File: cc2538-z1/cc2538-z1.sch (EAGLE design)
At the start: 89 parts, among them Q2 DMG6602SVT, U1 CC2538, U2 CC1120_RHM_32, U3 TPD2E001IDRLRQ1, U4 CP2103, U5 BSS138PS, U6 BSS138PS, U7 BSS138PS, X1 FA-128, X2 32MHz, X3 32.768K

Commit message: A lot of work on 4-layer CC2538/1120 design.
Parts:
- added C16, C17: 100nf, CC11x:C_EUC0603S
- added L5: BEAD, CC11x:L_US0603
- R11, R13: device resistor:R-EU_R0805 -> rcl:R-EU_R0603
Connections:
- removed net N$38: H1.ADC_3V3
- removed net N$47: H1.AGND
- removed net N$63: H1.CDP-3.3V
- new net +3V3_ANALOGUE: C17.1, H1.ADC_3V3, L5.1, U1.AVDD, U1.AVDD2, U1.AVDD3, U1.AVDD4, U1.AVDD5
- new net N$35: H1.ADC0
- new net N$36: H1.ADC3
- new net N$37: H1.ADC4
- new net N$39: H1.ADC6
- new net N$40: H1.ALERT
- net +3V3: now also C16.1, L5.2; no longer U1.AVDD, U1.AVDD2, U1.AVDD3, U1.AVDD4, U1.AVDD5
- net +3V3_SERIAL: now also H1.CDP-3.3V
- net GND: now also C16.2, C17.2, H1.AGND
- net SD_SPI_CLK: now also H1.CA1
- net SD_SPI_MISO: now also H1.TA1
- net SD_SPI_MOSI: now also H1.TA2
- net USER_BUTTON: now also H1.USER_INT
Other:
- moved on the sheet: C12, C13, X3

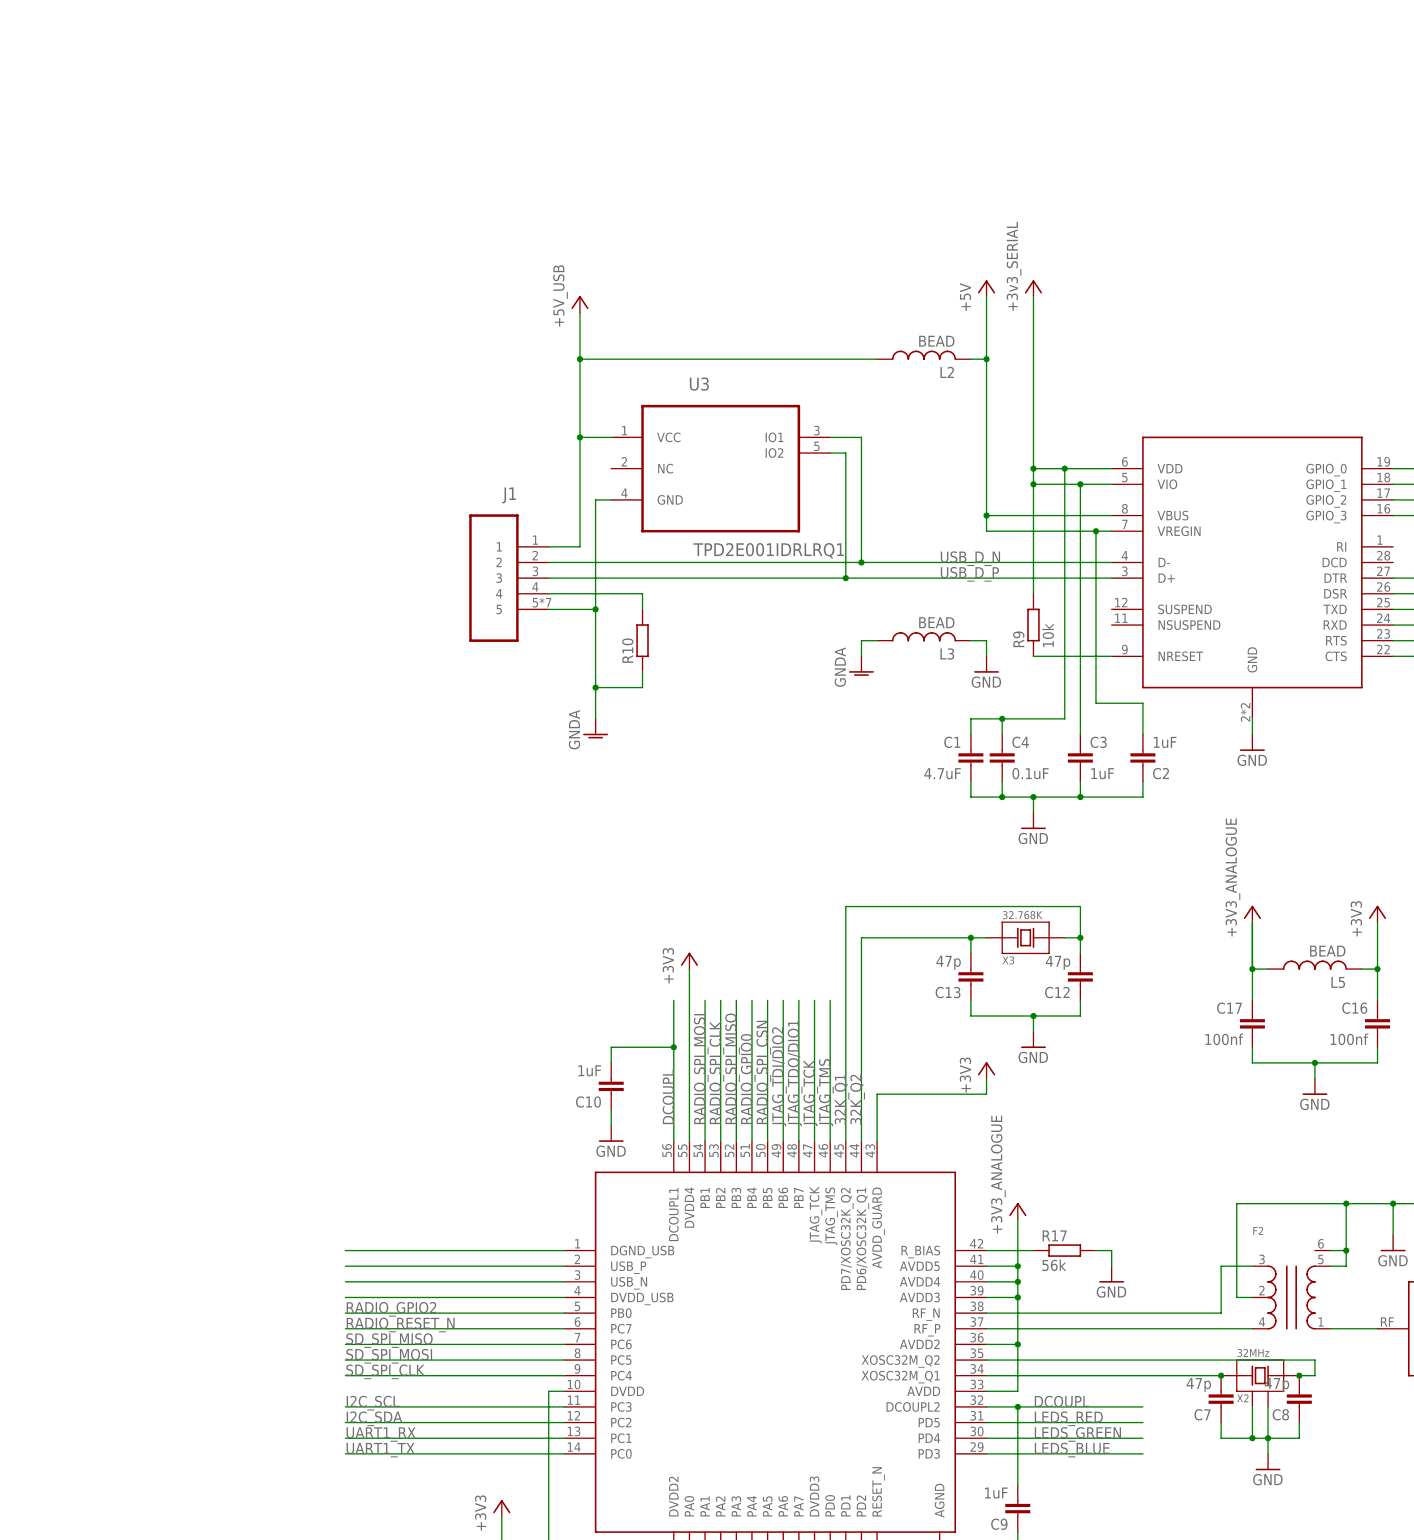
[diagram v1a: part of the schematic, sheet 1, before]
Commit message: Added Serial > 3v3 diode.
Added I2C pullup

still need to work out SD SEL
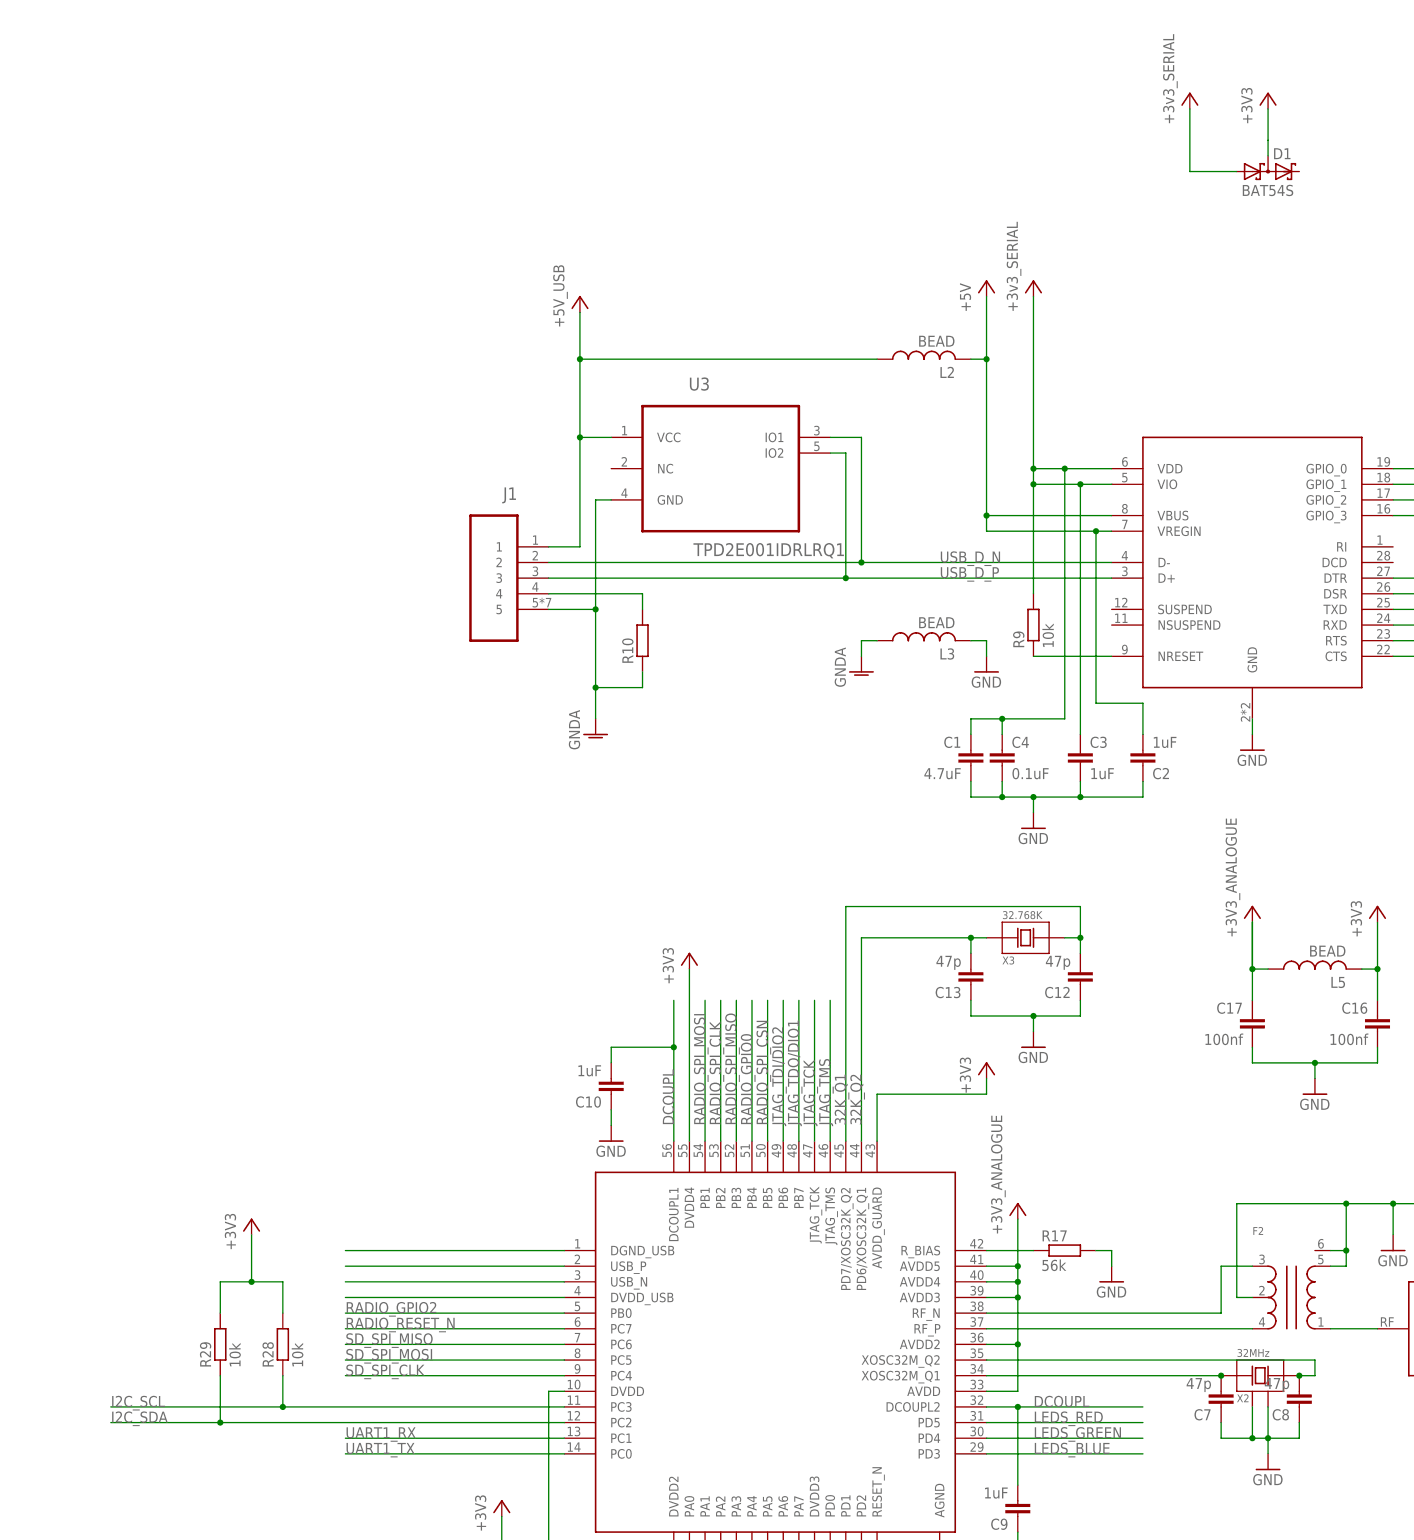
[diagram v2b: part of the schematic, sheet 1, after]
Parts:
- added D1: BAT54S, diode:BAT54S
- added R28, R29: 10k, rcl:R-EU_R0603
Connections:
- net +3V3: now also D1.C1A2, R28.2, R29.2
- net +3V3_SERIAL: now also D1.A1
- net I2C_SCL: now also R28.1
- net I2C_SDA: now also R29.1
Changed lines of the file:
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@@
 <part name="+3V13" library="supply1" deviceset="+3V3" device=""/>
 <part name="+3V14" library="supply1" deviceset="+3V3" device="" value="+3V3_ANALOGUE"/>
+<part name="R29" library="rcl" deviceset="R-EU_" device="R0603" value="10k"/>
+<part name="R28" library="rcl" deviceset="R-EU_" device="R0603" value="10k"/>
+<part name="+3V15" library="supply1" deviceset="+3V3" device=""/>
+<part name="+3V16" library="supply1" deviceset="+3V3" device=""/>
+<part name="+3V3_SERIAL2" library="supply1" deviceset="+3V3" device="" value="+3v3_SERIAL"/>
+<part name="D1" library="diode" deviceset="BAT54S" device=""/>
 </parts>
 <sheets>
@@
 <instance part="+3V13" gate="G$1" x="363.22" y="172.72"/>
 <instance part="+3V14" gate="G$1" x="304.8" y="124.46"/>
+<instance part="R29" gate="G$1" x="175.26" y="101.6" rot="R90"/>
+<instance part="R28" gate="G$1" x="185.42" y="101.6" rot="R90"/>
+<instance part="+3V15" gate="G$1" x="180.34" y="121.92"/>
+<instance part="+3V16" gate="G$1" x="345.44" y="304.8"/>
+<instance part="+3V3_SERIAL2" gate="G$1" x="332.74" y="304.8"/>
+<instance part="D1" gate="G$1" x="345.44" y="292.1"/>
 </instances>
 <busses>
@@
 <segment>
 <pinref part="U1" gate="G$1" pin="PC3"/>
-<wire x1="231.14" y1="91.44" x2="195.58" y2="91.44" width="0.1524" layer="91"/>
-<label x="195.58" y="91.44" size="1.778" layer="95"/>
+<wire x1="231.14" y1="91.44" x2="185.42" y2="91.44" width="0.1524" layer="91"/>
+<label x="157.48" y="91.44" size="1.778" layer="95"/>
+<pinref part="R28" gate="G$1" pin="1"/>
+<wire x1="185.42" y1="91.44" x2="185.42" y2="96.52" width="0.1524" layer="91"/>
+<wire x1="185.42" y1="91.44" x2="157.48" y2="91.44" width="0.1524" layer="91"/>
+<junction x="185.42" y="91.44"/>
 </segment>
 <segment>
@@
 <segment>
 <pinref part="U1" gate="G$1" pin="PC2"/>
-<wire x1="231.14" y1="88.9" x2="195.58" y2="88.9" width="0.1524" layer="91"/>
-<label x="195.58" y="88.9" size="1.778" layer="95"/>
+<wire x1="231.14" y1="88.9" x2="175.26" y2="88.9" width="0.1524" layer="91"/>
+<label x="157.48" y="88.9" size="1.778" layer="95"/>
+<pinref part="R29" gate="G$1" pin="1"/>
+<wire x1="175.26" y1="88.9" x2="175.26" y2="96.52" width="0.1524" layer="91"/>
+<wire x1="175.26" y1="88.9" x2="157.48" y2="88.9" width="0.1524" layer="91"/>
+<junction x="175.26" y="88.9"/>
 </segment>
 <segment>
@@
 <wire x1="363.22" y1="170.18" x2="363.22" y2="162.56" width="0.1524" layer="91"/>
 <junction x="363.22" y="162.56"/>
+</segment>
+<segment>
+<pinref part="R29" gate="G$1" pin="2"/>
+<wire x1="175.26" y1="106.68" x2="175.26" y2="111.76" width="0.1524" layer="91"/>
+<pinref part="+3V15" gate="G$1" pin="+3V3"/>
+<wire x1="175.26" y1="111.76" x2="180.34" y2="111.76" width="0.1524" layer="91"/>
+<wire x1="180.34" y1="111.76" x2="180.34" y2="119.38" width="0.1524" layer="91"/>
+<pinref part="R28" gate="G$1" pin="2"/>
+<wire x1="185.42" y1="106.68" x2="185.42" y2="111.76" width="0.1524" layer="91"/>
+<wire x1="185.42" y1="111.76" x2="180.34" y2="111.76" width="0.1524" layer="91"/>
+<junction x="180.34" y="111.76"/>
+</segment>
+<segment>
+<pinref part="+3V16" gate="G$1" pin="+3V3"/>
+<wire x1="345.44" y1="302.26" x2="345.44" y2="297.18" width="0.1524" layer="91"/>
+<pinref part="D1" gate="G$1" pin="C1A2"/>
+<wire x1="345.44" y1="294.64" x2="345.44" y2="297.18" width="0.1524" layer="91"/>
 </segment>
 </net>
@@
 <pinref part="+3V3_SERIAL1" gate="G$1" pin="+3V3"/>
 </segment>
-</net>
+<segment>
+<pinref part="+3V3_SERIAL2" gate="G$1" pin="+3V3"/>
+<wire x1="332.74" y1="302.26" x2="332.74" y2="292.1" width="0.1524" layer="91"/>
+<wire x1="332.74" y1="292.1" x2="340.36" y2="292.1" width="0.1524" layer="91"/>
+<pinref part="D1" gate="G$1" pin="A1"/>
+</segment>
+</net>

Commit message: plit schematic into separate pages & added framesy
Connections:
- net +5V: now also L2.1
- net +5V_USB: no longer L2.1

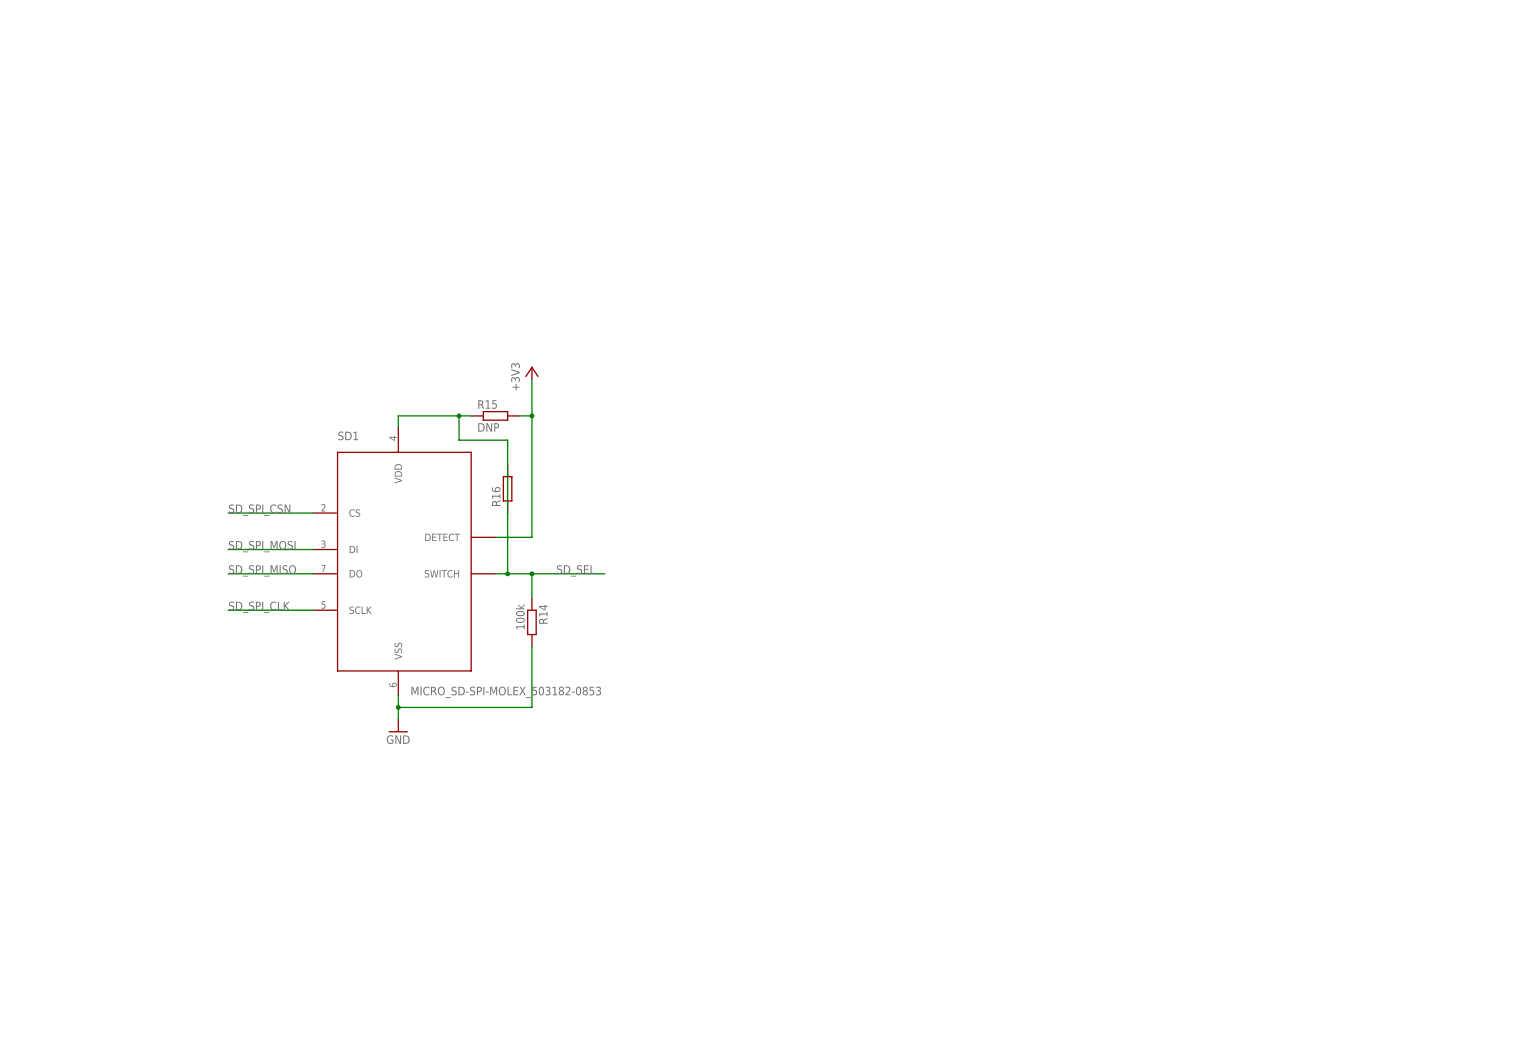
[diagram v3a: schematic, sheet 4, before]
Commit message: Added SPI Flash & moved 2.4G UFL
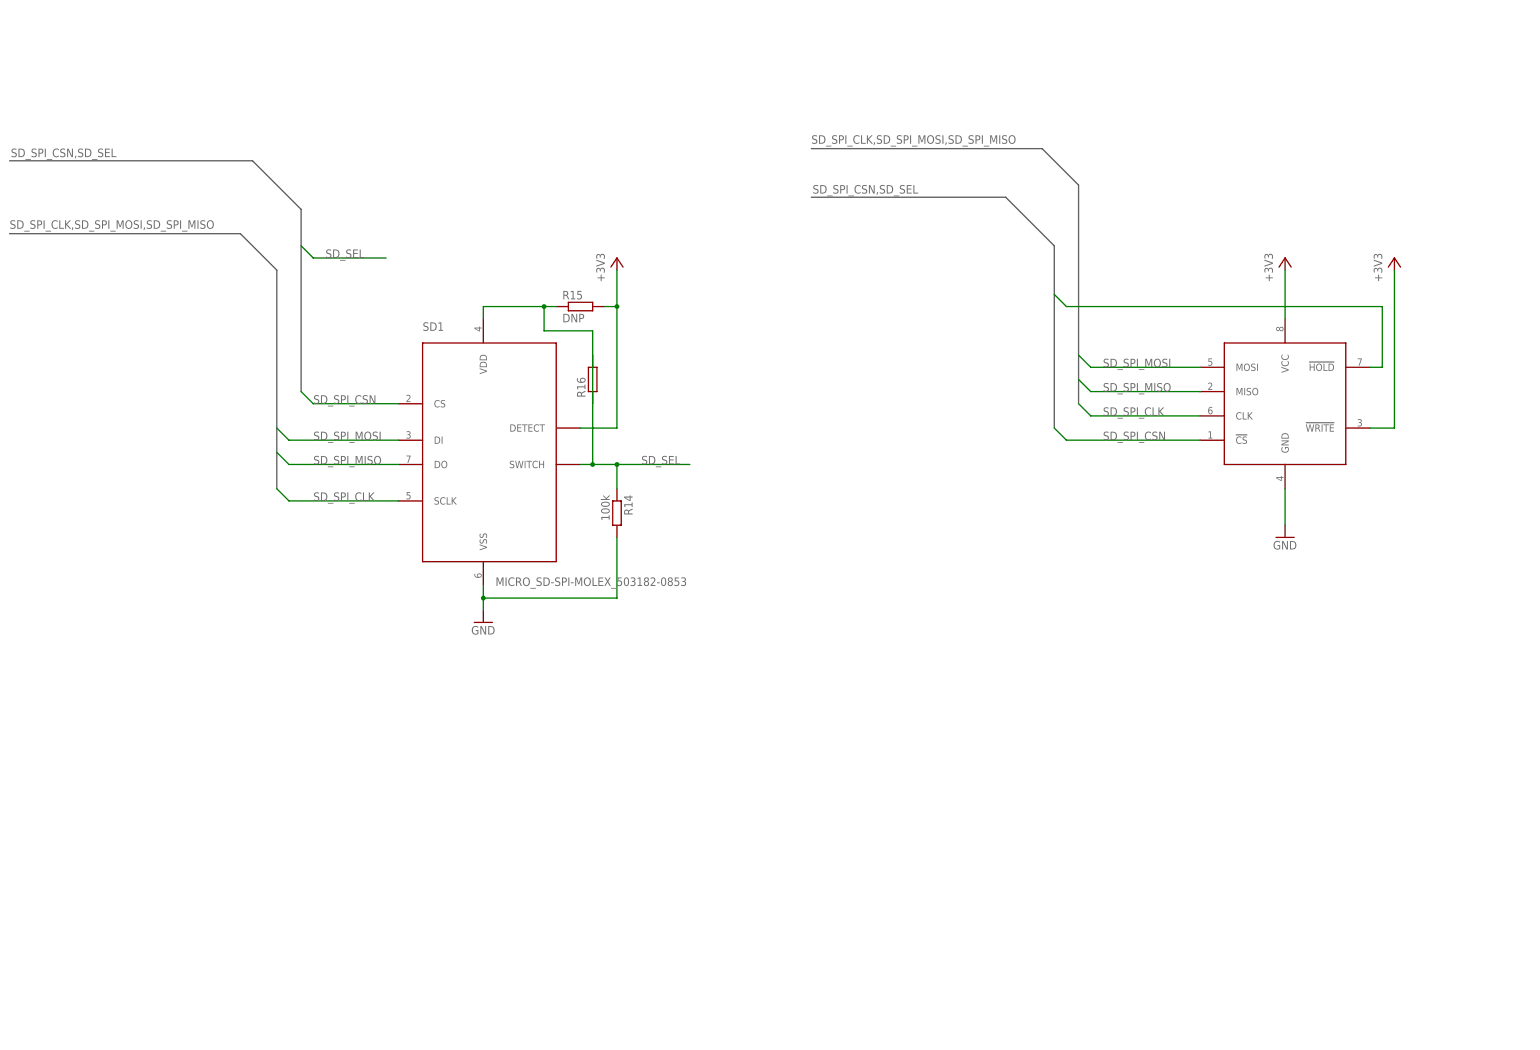
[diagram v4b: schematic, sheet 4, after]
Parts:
- added C18, C19: 100nf, CC11x:C_EUC0603S
- added LED_EN: (no value), CC11x:PINHD-1X2
- added U8: M25P16VMN6P, CC11x:M25P16VMN6P
- renumbered R8 to R7
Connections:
- new net N$38: H1.ADC5
- net +3V3: now also LED_EN.1, LED_EN.2, U8.!WRITE, U8.VCC
- net +5V: now also C19.1; no longer L2.1
- net +5V_USB: now also C18.1, L2.1
- net GND: now also C19.2, U8.GND
- net GNDA: now also C18.2
- net JTAG_TDI/DIO2: no longer H1.ADC5
- net RADIO_GPIO0: now also R2.1, R2.2; no longer R5.1, R5.2
- net RADIO_SPI_CLK: now also R4.1, R4.2; no longer R3.1, R3.2
- net RADIO_SPI_CSN: now also R1.1, R1.2; no longer R4.1, R4.2
- net RADIO_SPI_MISO: now also R3.1, R3.2; no longer R2.1, R2.2
- net RADIO_SPI_MOSI: now also R5.1, R5.2; no longer R1.1, R1.2
- net SD_SEL: now also U8.!HOLD
- net SD_SPI_CLK: now also U8.CLK
- net SD_SPI_CSN: now also U8.!CS
- net SD_SPI_MISO: now also U8.MISO
- net SD_SPI_MOSI: now also U8.MOSI
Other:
- moved on the sheet: R1, R14, R15, R16, R2, R3, R4, R5, SD1

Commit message: Routing finished? need to sanity check.
Check pull ups for SPI
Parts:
- added R8: 56k, rcl:R-EU_R0603
- added U10: DMG6602SVT, farnell-parts:DMG6602SVT
- R14: value 100k -> 100K
- R15: value DNP -> 100K
- R16: value (none) -> DNP
- R17: value 56k -> DNP
- renumbered Q2 to U9
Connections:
- removed net JTAG_TDI/DIO2: H4.8, U1.PB6
- removed net JTAG_TDO/DIO1: H1.TA0, H4.6, U1.PB7
- removed net SD_SEL: R14.1, R15.1, R16.1, R16.2, SD1.SWITCH, SD1.VDD, U1.PA6, U8.!HOLD
- new net JTAG_TDI/FLASH_SPI_CSN: H4.8, U1.PB6, U8.!CS
- new net JTAG_TDO/SD_PRESENCE: H4.6, R17.2, SD1.DETECT, U1.PB7
- new net MEM_VCC: R16.1, R16.2, R17.1, SD1.VDD, U10G$2.D, U8.!HOLD, U8.!WRITE, U8.VCC
- new net N$41: H1.TA0
- new net N$43: R15.1, U10G$1.D@1, U10G$2.G
- new net PWR_MEM_EN: R14.2, U1.PA6, U10G$1.G
- net +3V3: now also U10G$2.S; no longer SD1.DETECT, U8.!WRITE, U8.VCC
- net GND: now also R14.1, R8.2, SD1.SWITCH, U10G$1.S; no longer R14.2, R17.2
- net N$21: now also R8.1; no longer R17.1
- net SD_SPI_CSN: no longer U8.!CS
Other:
- moved on the sheet: R14, R15, R16, SD1
